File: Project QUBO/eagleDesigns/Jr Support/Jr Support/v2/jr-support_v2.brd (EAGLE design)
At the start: 205.7 x 127 mm, 255 parts, among them IC1 74LVC1G08DBV, IC2 TLC2272PW, IC3 74LVC1G08DBV, IC4 74LVC1G08DBV, Q1 FDN5618P, U1 PCA9685, U2 LT3063, U3 LT3063

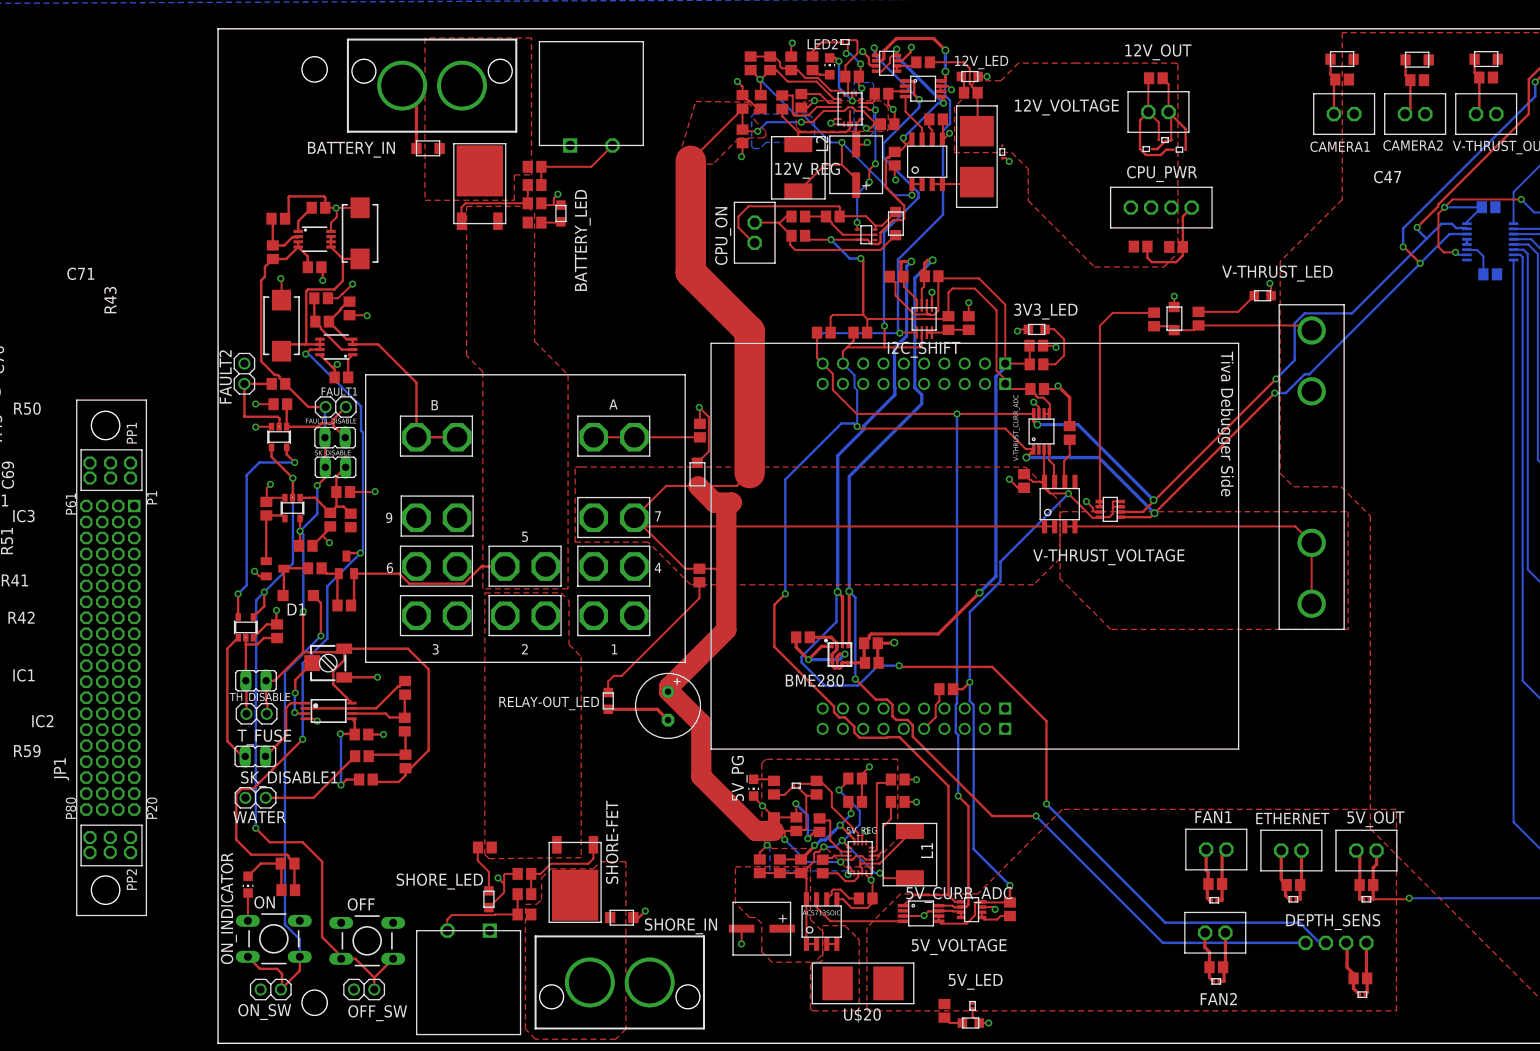
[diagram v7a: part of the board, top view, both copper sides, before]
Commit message: 
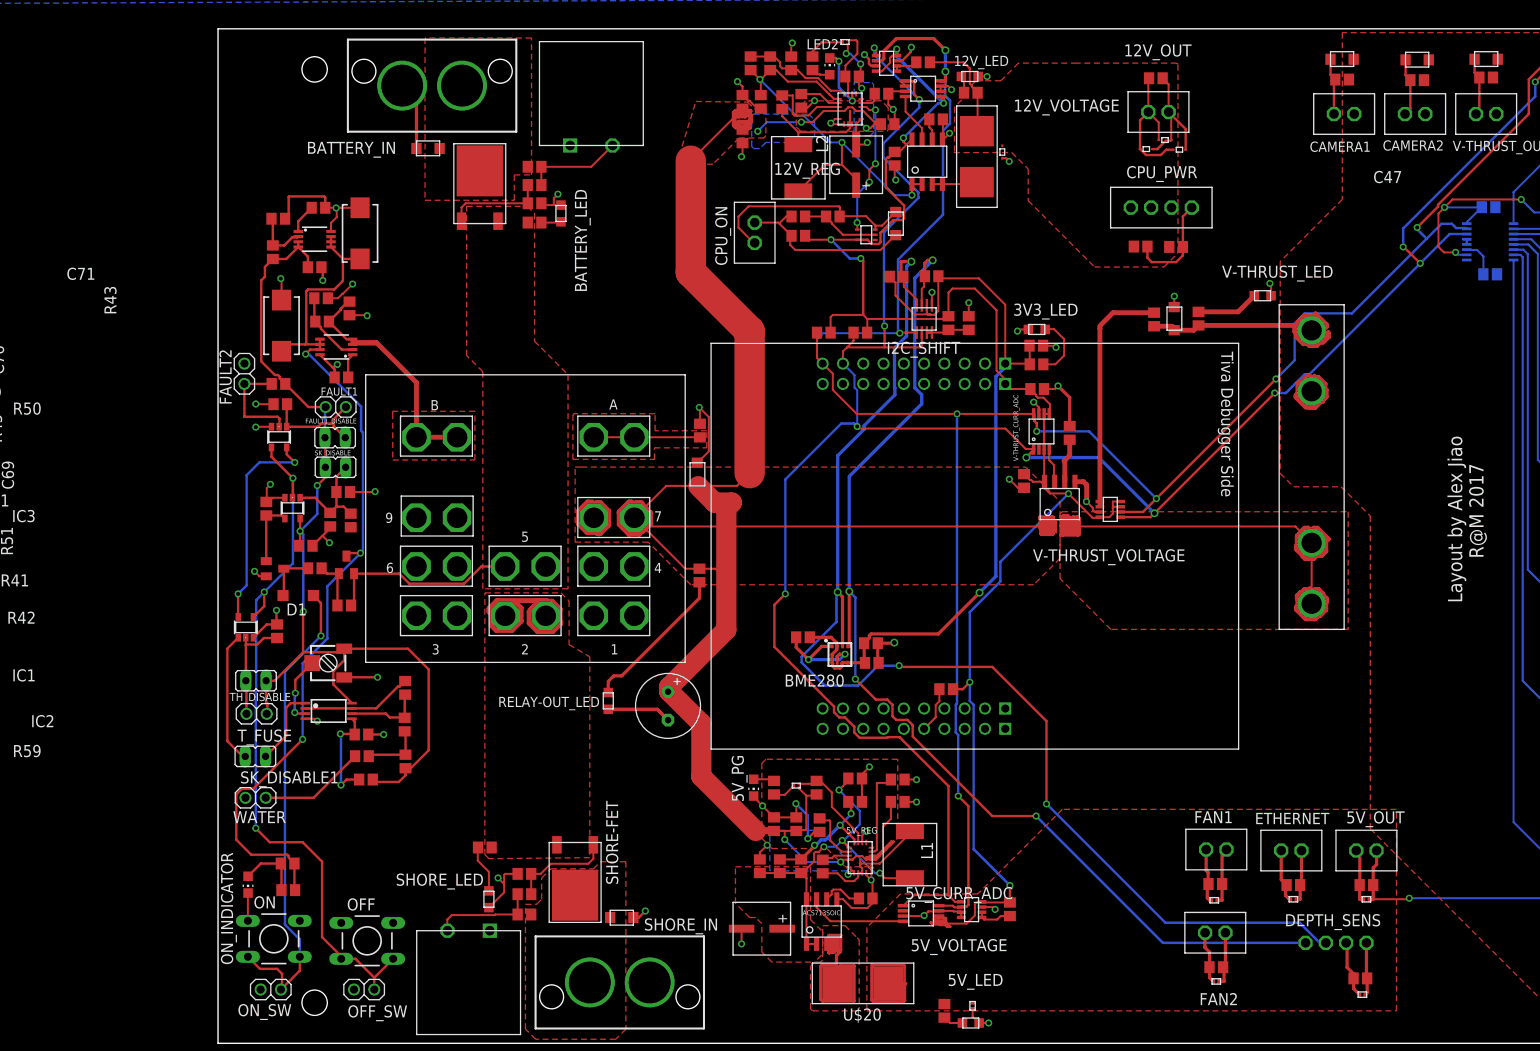
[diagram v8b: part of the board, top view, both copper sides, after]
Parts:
- removed JP1: (no value), samtec:MPSC-01-80
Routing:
- net RELAY_OUT: track 302.2 -> 362.0 mm
- net N$34: track 39.4 -> 83.2 mm
- net V_THRUST: track 20.4 -> 59.2 mm
- net N$55: track 1.27 -> 34.7 mm
- net RELAY-SHORE: track 0.00 -> 32.5 mm
- net 5V: track 544.3 -> 576.6 mm
- net N$58: track 30.1 -> 52.1 mm
- net RELAY-CTRL: track 30.1 -> 52.1 mm
- net GND: track 494.1 -> 505.5 mm
- net SDA1: track 363.2 -> 364.0 mm
- added copper zone on layer 1, net N$35
- added copper zone on layer 1, net RELAY-CTRL
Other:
- board text added: "Layout by Alex Jiao R@M 2017"
